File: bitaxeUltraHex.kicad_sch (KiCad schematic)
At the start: 12 parts, among them J1 Conn_01x01, J2 Conn_01x01

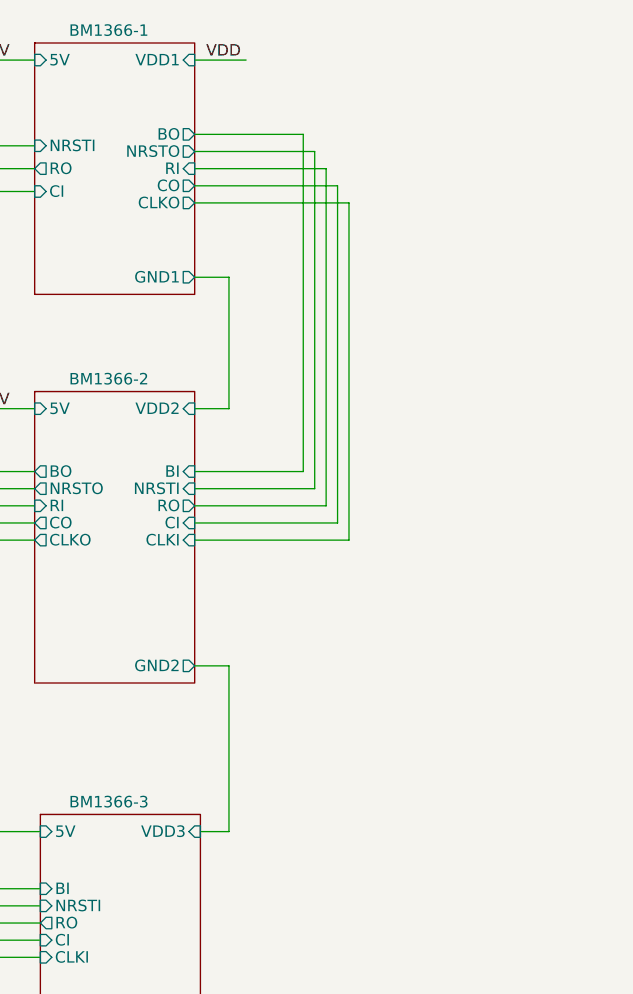
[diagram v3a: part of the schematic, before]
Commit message: Replace reference voltage regulators with new one
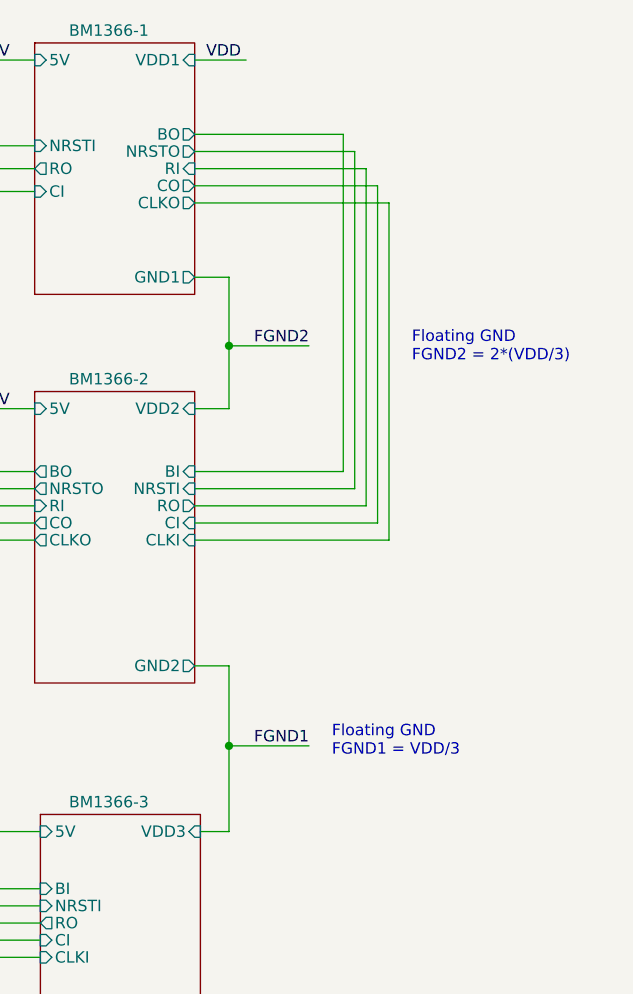
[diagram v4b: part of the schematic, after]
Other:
- note added: "Floating GND FGND1 = VDD/3"
- note added: "Floating GND FGND2 = 2*(VDD/3)"
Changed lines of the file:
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@@
     (rev "1")
   )
+  (junction (at 172.72 106.68) (diameter 0) (color 0 0 0 0)
+  )
+  (junction (at 172.72 62.23) (diameter 0) (color 0 0 0 0)
+  )
   (junction (at 102.235 80.01) (diameter 0) (color 0 0 0 0)
   )
@@
     (stroke (width 0) (type default))
   )
-  (wire (pts (xy 184.785 44.45) (xy 184.785 81.915))
+  (wire (pts (xy 189.23 44.45) (xy 189.23 81.915))
     (stroke (width 0) (type default))
   )
@@
     (stroke (width 0) (type default))
   )
-  (wire (pts (xy 168.91 46.355) (xy 186.055 46.355))
+  (wire (pts (xy 172.72 106.68) (xy 172.72 116.205))
+    (stroke (width 0) (type default))
+  )
+  (wire (pts (xy 168.91 46.355) (xy 190.5 46.355))
     (stroke (width 0) (type default))
   )
@@
     (stroke (width 0) (type default))
   )
-  (wire (pts (xy 168.91 42.545) (xy 183.515 42.545))
+  (wire (pts (xy 168.91 42.545) (xy 187.96 42.545))
     (stroke (width 0) (type default))
   )
@@
     (stroke (width 0) (type default))
   )
-  (wire (pts (xy 183.515 42.545) (xy 183.515 80.01))
+  (wire (pts (xy 187.96 42.545) (xy 187.96 80.01))
     (stroke (width 0) (type default))
   )
@@
     (stroke (width 0) (type default))
   )
+  (wire (pts (xy 172.72 62.23) (xy 172.72 69.215))
+    (stroke (width 0) (type default))
+  )
   (wire (pts (xy 117.475 45.085) (xy 117.475 90.805))
     (stroke (width 0) (type default))
@@
     (stroke (width 0) (type default))
   )
-  (wire (pts (xy 168.91 38.735) (xy 180.975 38.735))
-    (stroke (width 0) (type default))
-  )
-  (wire (pts (xy 180.975 76.2) (xy 168.91 76.2))
+  (wire (pts (xy 168.91 38.735) (xy 185.42 38.735))
+    (stroke (width 0) (type default))
+  )
+  (wire (pts (xy 185.42 76.2) (xy 168.91 76.2))
     (stroke (width 0) (type default))
   )
@@
     (stroke (width 0) (type default))
   )
-  (wire (pts (xy 168.91 44.45) (xy 184.785 44.45))
+  (wire (pts (xy 168.91 44.45) (xy 189.23 44.45))
     (stroke (width 0) (type default))
   )
@@
     (stroke (width 0) (type default))
   )
-  (wire (pts (xy 186.055 46.355) (xy 186.055 83.82))
-    (stroke (width 0) (type default))
-  )
-  (wire (pts (xy 186.055 83.82) (xy 168.91 83.82))
-    (stroke (width 0) (type default))
-  )
-  (wire (pts (xy 180.975 38.735) (xy 180.975 76.2))
+  (wire (pts (xy 190.5 46.355) (xy 190.5 83.82))
+    (stroke (width 0) (type default))
+  )
+  (wire (pts (xy 190.5 83.82) (xy 168.91 83.82))
+    (stroke (width 0) (type default))
+  )
+  (wire (pts (xy 185.42 38.735) (xy 185.42 76.2))
     (stroke (width 0) (type default))
   )
@@
     (stroke (width 0) (type default))
   )
-  (wire (pts (xy 182.245 40.64) (xy 168.91 40.64))
+  (wire (pts (xy 186.69 40.64) (xy 168.91 40.64))
     (stroke (width 0) (type default))
   )
@@
     (stroke (width 0) (type default))
   )
-  (wire (pts (xy 182.245 78.105) (xy 182.245 40.64))
+  (wire (pts (xy 186.69 78.105) (xy 186.69 40.64))
     (stroke (width 0) (type default))
   )
@@
     (stroke (width 0) (type default))
   )
+  (wire (pts (xy 172.72 106.68) (xy 181.61 106.68))
+    (stroke (width 0) (type default))
+  )
   (wire (pts (xy 133.985 80.01) (xy 133.985 126.365))
     (stroke (width 0) (type default))
   )
+  (wire (pts (xy 172.72 62.23) (xy 181.61 62.23))
+    (stroke (width 0) (type default))
+  )
   (wire (pts (xy 102.235 42.545) (xy 102.235 80.01))
     (stroke (width 0) (type default))
   )
-  (wire (pts (xy 183.515 80.01) (xy 168.91 80.01))
-    (stroke (width 0) (type default))
-  )
-  (wire (pts (xy 172.72 54.61) (xy 172.72 69.215))
+  (wire (pts (xy 187.96 80.01) (xy 168.91 80.01))
+    (stroke (width 0) (type default))
+  )
+  (wire (pts (xy 172.72 54.61) (xy 172.72 62.23))
     (stroke (width 0) (type default))
   )
@@
     (stroke (width 0) (type default))
   )
-  (wire (pts (xy 172.72 97.79) (xy 172.72 116.205))
+  (wire (pts (xy 172.72 97.79) (xy 172.72 106.68))
     (stroke (width 0) (type default))
   )
@@
     (stroke (width 0) (type default))
   )
-  (wire (pts (xy 184.785 81.915) (xy 168.91 81.915))
+  (wire (pts (xy 189.23 81.915) (xy 168.91 81.915))
     (stroke (width 0) (type default))
   )
@@
     (stroke (width 0) (type default))
   )
-  (wire (pts (xy 168.91 78.105) (xy 182.245 78.105))
+  (wire (pts (xy 168.91 78.105) (xy 186.69 78.105))
     (stroke (width 0) (type default))
   )
@@
     (effects (font (size 1.27 1.27)) (justify left bottom))
   )
+  (text "Floating GND\nFGND1 = VDD/3" (at 184.15 107.95 0)
+    (effects (font (size 1.27 1.27)) (justify left bottom))
+  )
+  (text "Floating GND\nFGND2 = 2*(VDD/3)" (at 193.04 64.135 0)
+    (effects (font (size 1.27 1.27)) (justify left bottom))
+  )
+  (label "FGND1" (at 181.61 106.68 180) (fields_autoplaced)
+    (effects (font (size 1.27 1.27)) (justify right bottom))
+  )
   (label "5V" (at 146.05 30.48 0) (fields_autoplaced)
     (effects (font (size 1.27 1.27)) (justify left bottom))
@@
     (effects (font (size 1.27 1.27)) (justify left bottom))
   )
+  (label "FGND2" (at 181.61 62.23 180) (fields_autoplaced)
+    (effects (font (size 1.27 1.27)) (justify right bottom))
+  )
   (label "3V3" (at 61.595 73.66 0) (fields_autoplaced)

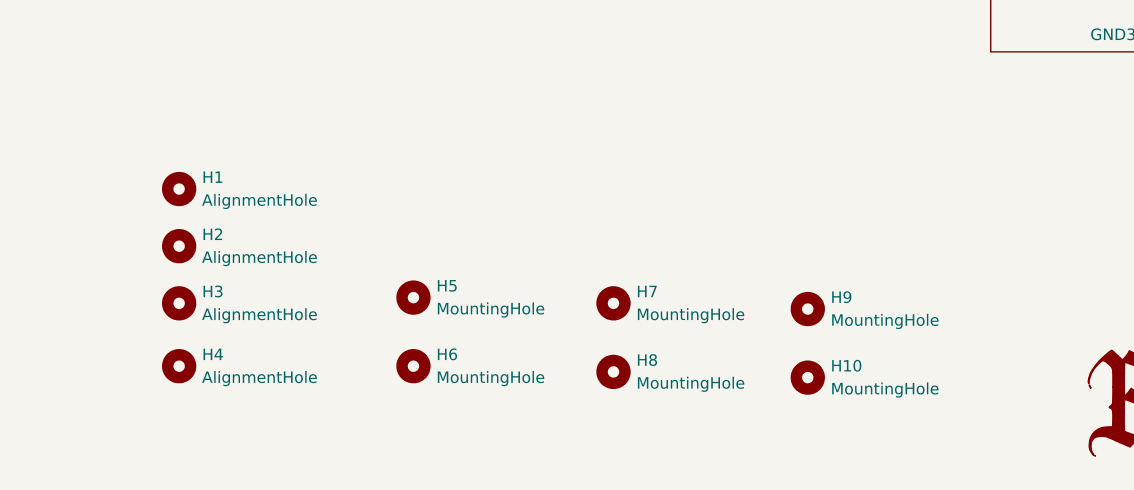
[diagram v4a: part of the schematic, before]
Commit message: changed USB connector to USB C. updated display.
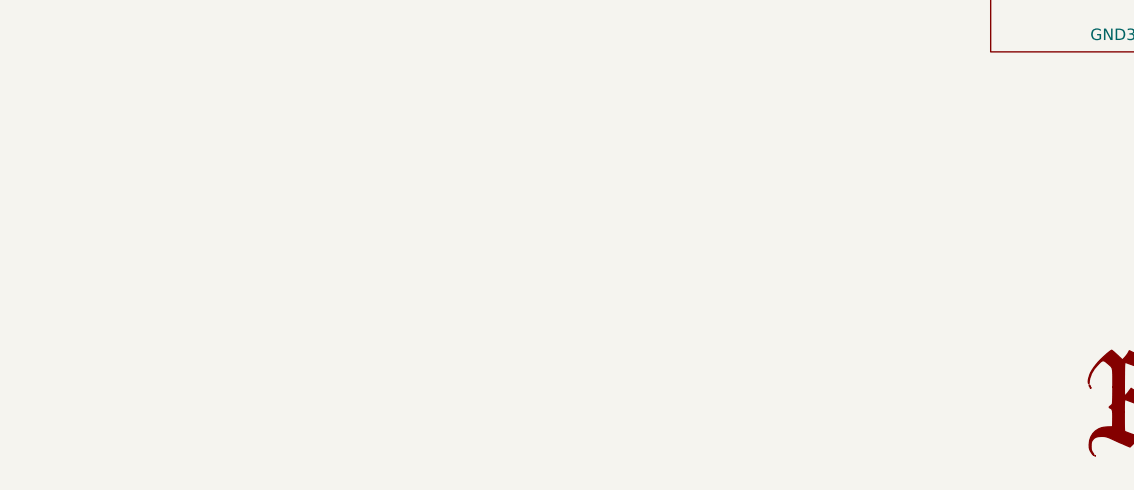
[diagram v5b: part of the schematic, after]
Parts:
- removed H1, H2, H3, H4: AlignmentHole, MountingHole:MountingHole_2.2mm_M2, symbol Mechanical:MountingHole
- removed H10, H5, H6, H7, H8, H9: MountingHole, MountingHole:MountingHole_3.5mm, symbol Mechanical:MountingHole
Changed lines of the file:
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@@
-    )
-  )
-  (symbol (lib_id "Mechanical:MountingHole") (at 61.595 168.91 0) (unit 1)
-    (in_bom no) (on_board yes) (dnp no) (fields_autoplaced)
-    (property "Reference" "H3" (at 64.135 167.6399 0)
-      (effects (font (size 1.27 1.27)) (justify left))
-    )
-    (property "Value" "AlignmentHole" (at 64.135 170.1799 0)
-      (effects (font (size 1.27 1.27)) (justify left))
-    )
-    (property "Footprint" "MountingHole:MountingHole_2.2mm_M2" (at 61.595 168.91 0)
-      (effects (font (size 1.27 1.27)) hide)
-    )
-    (property "Datasheet" "~" (at 61.595 168.91 0)
-      (effects (font (size 1.27 1.27)) hide)
-    )
-    (property "PARTNO" "https://www.amazon.com/dp/B07MDFS1YS" (at 61.595 168.91 0)
-      (effects (font (size 1.27 1.27)) hide)
-    )
-    (instances
-      (project "bitaxeUltraHex"
-        (path "/e63e39d7-6ac0-4ffd-8aa3-1841a4541b55"
-          (reference "H3") (unit 1)
-        )
-      )
-    )
-  )
-  (symbol (lib_id "Mechanical:MountingHole") (at 109.855 168.91 0) (unit 1)
-    (in_bom no) (on_board yes) (dnp no) (fields_autoplaced)
-    (property "Reference" "H7" (at 112.395 167.6399 0)
-      (effects (font (size 1.27 1.27)) (justify left))
-    )
-    (property "Value" "MountingHole" (at 112.395 170.1799 0)
-      (effects (font (size 1.27 1.27)) (justify left))
-    )
-    (property "Footprint" "MountingHole:MountingHole_3.5mm" (at 109.855 168.91 0)
-      (effects (font (size 1.27 1.27)) hide)
-    )
-    (property "Datasheet" "~" (at 109.855 168.91 0)
-      (effects (font (size 1.27 1.27)) hide)
-    )
-    (instances
-      (project "bitaxeUltraHex"
-        (path "/e63e39d7-6ac0-4ffd-8aa3-1841a4541b55"
-          (reference "H7") (unit 1)
-        )
-      )
-    )
-  )
-  (symbol (lib_id "Mechanical:MountingHole") (at 131.445 177.165 0) (unit 1)
-    (in_bom no) (on_board yes) (dnp no) (fields_autoplaced)
-    (property "Reference" "H10" (at 133.985 175.8949 0)
-      (effects (font (size 1.27 1.27)) (justify left))
-    )
-    (property "Value" "MountingHole" (at 133.985 178.4349 0)
-      (effects (font (size 1.27 1.27)) (justify left))
-    )
-    (property "Footprint" "MountingHole:MountingHole_3.5mm" (at 131.445 177.165 0)
-      (effects (font (size 1.27 1.27)) hide)
-    )
-    (property "Datasheet" "~" (at 131.445 177.165 0)
-      (effects (font (size 1.27 1.27)) hide)
-    )
-    (instances
-      (project "bitaxeUltraHex"
-        (path "/e63e39d7-6ac0-4ffd-8aa3-1841a4541b55"
-          (reference "H10") (unit 1)
-        )
-      )
-    )
-  )
-  (symbol (lib_id "Mechanical:MountingHole") (at 109.855 176.53 0) (unit 1)
-    (in_bom no) (on_board yes) (dnp no) (fields_autoplaced)
-    (property "Reference" "H8" (at 112.395 175.2599 0)
-      (effects (font (size 1.27 1.27)) (justify left))
-    )
-    (property "Value" "MountingHole" (at 112.395 177.7999 0)
-      (effects (font (size 1.27 1.27)) (justify left))
-    )
-    (property "Footprint" "MountingHole:MountingHole_3.5mm" (at 109.855 176.53 0)
-      (effects (font (size 1.27 1.27)) hide)
-    )
-    (property "Datasheet" "~" (at 109.855 176.53 0)
-      (effects (font (size 1.27 1.27)) hide)
-    )
-    (instances
-      (project "bitaxeUltraHex"
-        (path "/e63e39d7-6ac0-4ffd-8aa3-1841a4541b55"
-          (reference "H8") (unit 1)
-        )
-      )
     )
   )
@@
         (path "/e63e39d7-6ac0-4ffd-8aa3-1841a4541b55"
           (reference "#G1") (unit 1)
-        )
-      )
-    )
-  )
-  (symbol (lib_id "Mechanical:MountingHole") (at 61.595 162.56 0) (unit 1)
-    (in_bom no) (on_board yes) (dnp no) (fields_autoplaced)
-    (property "Reference" "H2" (at 64.135 161.2899 0)
-      (effects (font (size 1.27 1.27)) (justify left))
-    )
-    (property "Value" "AlignmentHole" (at 64.135 163.8299 0)
-      (effects (font (size 1.27 1.27)) (justify left))
-    )
-    (property "Footprint" "MountingHole:MountingHole_2.2mm_M2" (at 61.595 162.56 0)
-      (effects (font (size 1.27 1.27)) hide)
-    )
-    (property "Datasheet" "~" (at 61.595 162.56 0)
-      (effects (font (size 1.27 1.27)) hide)
-    )
-    (property "PARTNO" "https://www.amazon.com/dp/B07MDFS1YS" (at 61.595 162.56 0)
-      (effects (font (size 1.27 1.27)) hide)
-    )
-    (instances
-      (project "bitaxeUltraHex"
-        (path "/e63e39d7-6ac0-4ffd-8aa3-1841a4541b55"
-          (reference "H2") (unit 1)
         )
       )
@@
         )
       )
-    )
-  )
-  (symbol (lib_id "Mechanical:MountingHole") (at 61.595 156.21 0) (unit 1)
-    (in_bom no) (on_board yes) (dnp no) (fields_autoplaced)
-    (property "Reference" "H1" (at 64.135 154.9399 0)
-      (effects (font (size 1.27 1.27)) (justify left))
-    )
-    (property "Value" "AlignmentHole" (at 64.135 157.4799 0)
-      (effects (font (size 1.27 1.27)) (justify left))
-    )
-    (property "Footprint" "MountingHole:MountingHole_2.2mm_M2" (at 61.595 156.21 0)
-      (effects (font (size 1.27 1.27)) hide)
-    )
-    (property "Datasheet" "~" (at 61.595 156.21 0)
-      (effects (font (size 1.27 1.27)) hide)
-    )
-    (property "PARTNO" "https://www.amazon.com/dp/B07MDFS1YS" (at 61.595 156.21 0)
-      (effects (font (size 1.27 1.27)) hide)
-    )
-    (instances
-      (project "bitaxeUltraHex"
-        (path "/e63e39d7-6ac0-4ffd-8aa3-1841a4541b55"
-          (reference "H1") (unit 1)
-        )
-      )
-    )
-  )
-  (symbol (lib_id "Mechanical:MountingHole") (at 87.63 175.895 0) (unit 1)
-    (in_bom no) (on_board yes) (dnp no) (fields_autoplaced)
-    (property "Reference" "H6" (at 90.17 174.6249 0)
-      (effects (font (size 1.27 1.27)) (justify left))
-    )
-    (property "Value" "MountingHole" (at 90.17 177.1649 0)
-      (effects (font (size 1.27 1.27)) (justify left))
-    )
-    (property "Footprint" "MountingHole:MountingHole_3.5mm" (at 87.63 175.895 0)
-      (effects (font (size 1.27 1.27)) hide)
-    )
-    (property "Datasheet" "~" (at 87.63 175.895 0)
-      (effects (font (size 1.27 1.27)) hide)
-    )
-    (instances
-      (project "bitaxeUltraHex"
-        (path "/e63e39d7-6ac0-4ffd-8aa3-1841a4541b55"
-          (reference "H6") (unit 1)
-        )
-      )
-    )
-  )
-  (symbol (lib_id "Mechanical:MountingHole") (at 87.63 168.275 0) (unit 1)
-    (in_bom no) (on_board yes) (dnp no) (fields_autoplaced)
-    (property "Reference" "H5" (at 90.17 167.0049 0)
-      (effects (font (size 1.27 1.27)) (justify left))
-    )
-    (property "Value" "MountingHole" (at 90.17 169.5449 0)
-      (effects (font (size 1.27 1.27)) (justify left))
-    )
-    (property "Footprint" "MountingHole:MountingHole_3.5mm" (at 87.63 168.275 0)
-      (effects (font (size 1.27 1.27)) hide)
-    )
-    (property "Datasheet" "~" (at 87.63 168.275 0)
-      (effects (font (size 1.27 1.27)) hide)
-    )
-    (instances
-      (project "bitaxeUltraHex"
-        (path "/e63e39d7-6ac0-4ffd-8aa3-1841a4541b55"
-          (reference "H5") (unit 1)
-        )
-      )
-    )
-  )
-  (symbol (lib_id "Mechanical:MountingHole") (at 131.445 169.545 0) (unit 1)
-    (in_bom no) (on_board yes) (dnp no) (fields_autoplaced)
-    (property "Reference" "H9" (at 133.985 168.2749 0)
-      (effects (font (size 1.27 1.27)) (justify left))
-    )
-    (property "Value" "MountingHole" (at 133.985 170.8149 0)
-      (effects (font (size 1.27 1.27)) (justify left))
-    )
-    (property "Footprint" "MountingHole:MountingHole_3.5mm" (at 131.445 169.545 0)
-      (effects (font (size 1.27 1.27)) hide)
-    )
-    (property "Datasheet" "~" (at 131.445 169.545 0)
-      (effects (font (size 1.27 1.27)) hide)
-    )
-    (instances
-      (project "bitaxeUltraHex"
-        (path "/e63e39d7-6ac0-4ffd-8aa3-1841a4541b55"
-          (reference "H9") (unit 1)
-        )
-      )
-    )
-  )
-  (symbol (lib_id "Mechanical:MountingHole") (at 61.595 175.895 0) (unit 1)
-    (in_bom no) (on_board yes) (dnp no) (fields_autoplaced)
-    (property "Reference" "H4" (at 64.135 174.6249 0)
-      (effects (font (size 1.27 1.27)) (justify left))
-    )
-    (property "Value" "AlignmentHole" (at 64.135 177.1649 0)
-      (effects (font (size 1.27 1.27)) (justify left))
-    )
-    (property "Footprint" "MountingHole:MountingHole_2.2mm_M2" (at 61.595 175.895 0)
-      (effects (font (size 1.27 1.27)) hide)
-    )
-    (property "Datasheet" "~" (at 61.595 175.895 0)
-      (effects (font (size 1.27 1.27)) hide)
-    )
-    (property "PARTNO" "https://www.amazon.com/dp/B07MDFS1YS" (at 61.595 175.895 0)
-      (effects (font (size 1.27 1.27)) hide)
-    )
-    (instances
-      (project "bitaxeUltraHex"
-        (path "/e63e39d7-6ac0-4ffd-8aa3-1841a4541b55"
-          (reference "H4") (unit 1)
-        )
-      )
